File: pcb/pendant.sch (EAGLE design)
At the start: 55 parts, among them CON1 USB_MICROSMT+THRUHULE, Q2 16MHz, SW2 BUTTON_2, T1 SSM3J328R,LF, T2 SSM3J328R,LF, U2 MK20D--VFM5, U3 74LVC1G17DCK, U4 74LVC1G17DCK

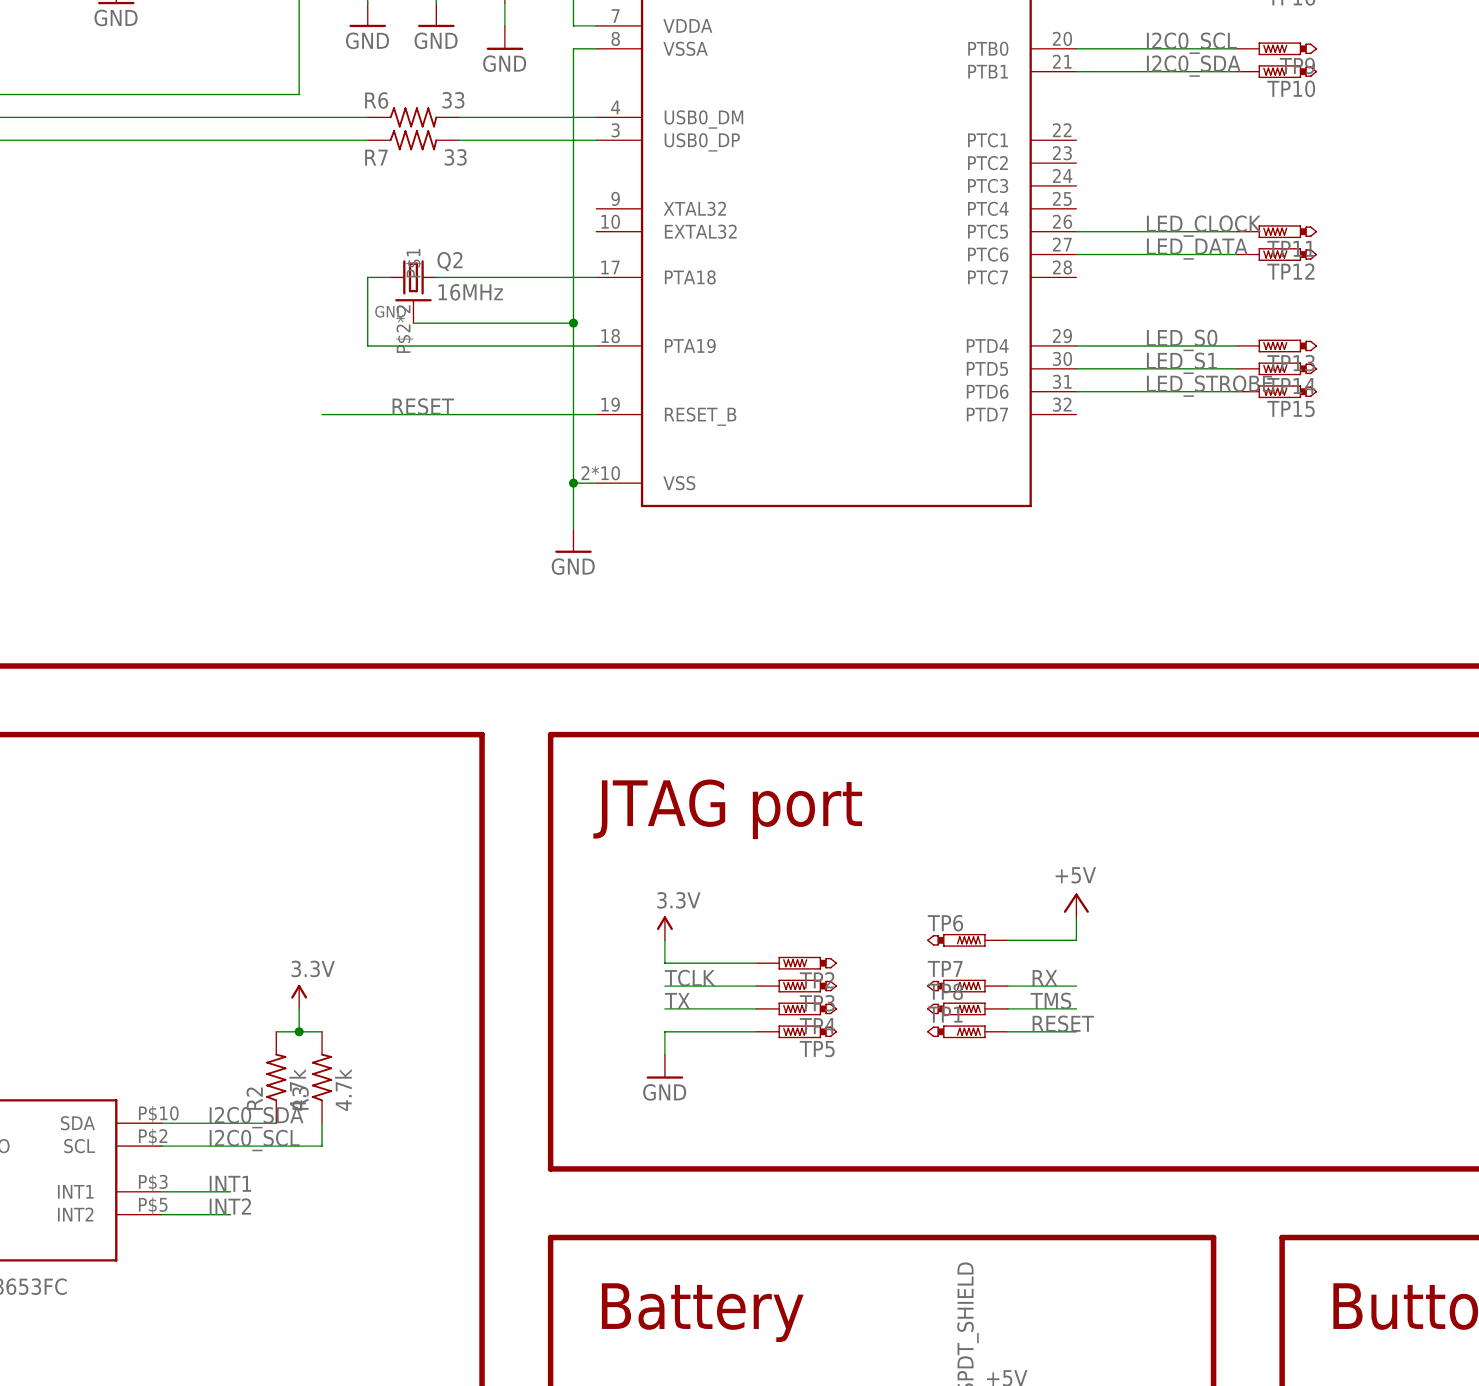
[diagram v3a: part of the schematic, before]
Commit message: Add interrupt line from accelerometer, clean up test pad positions
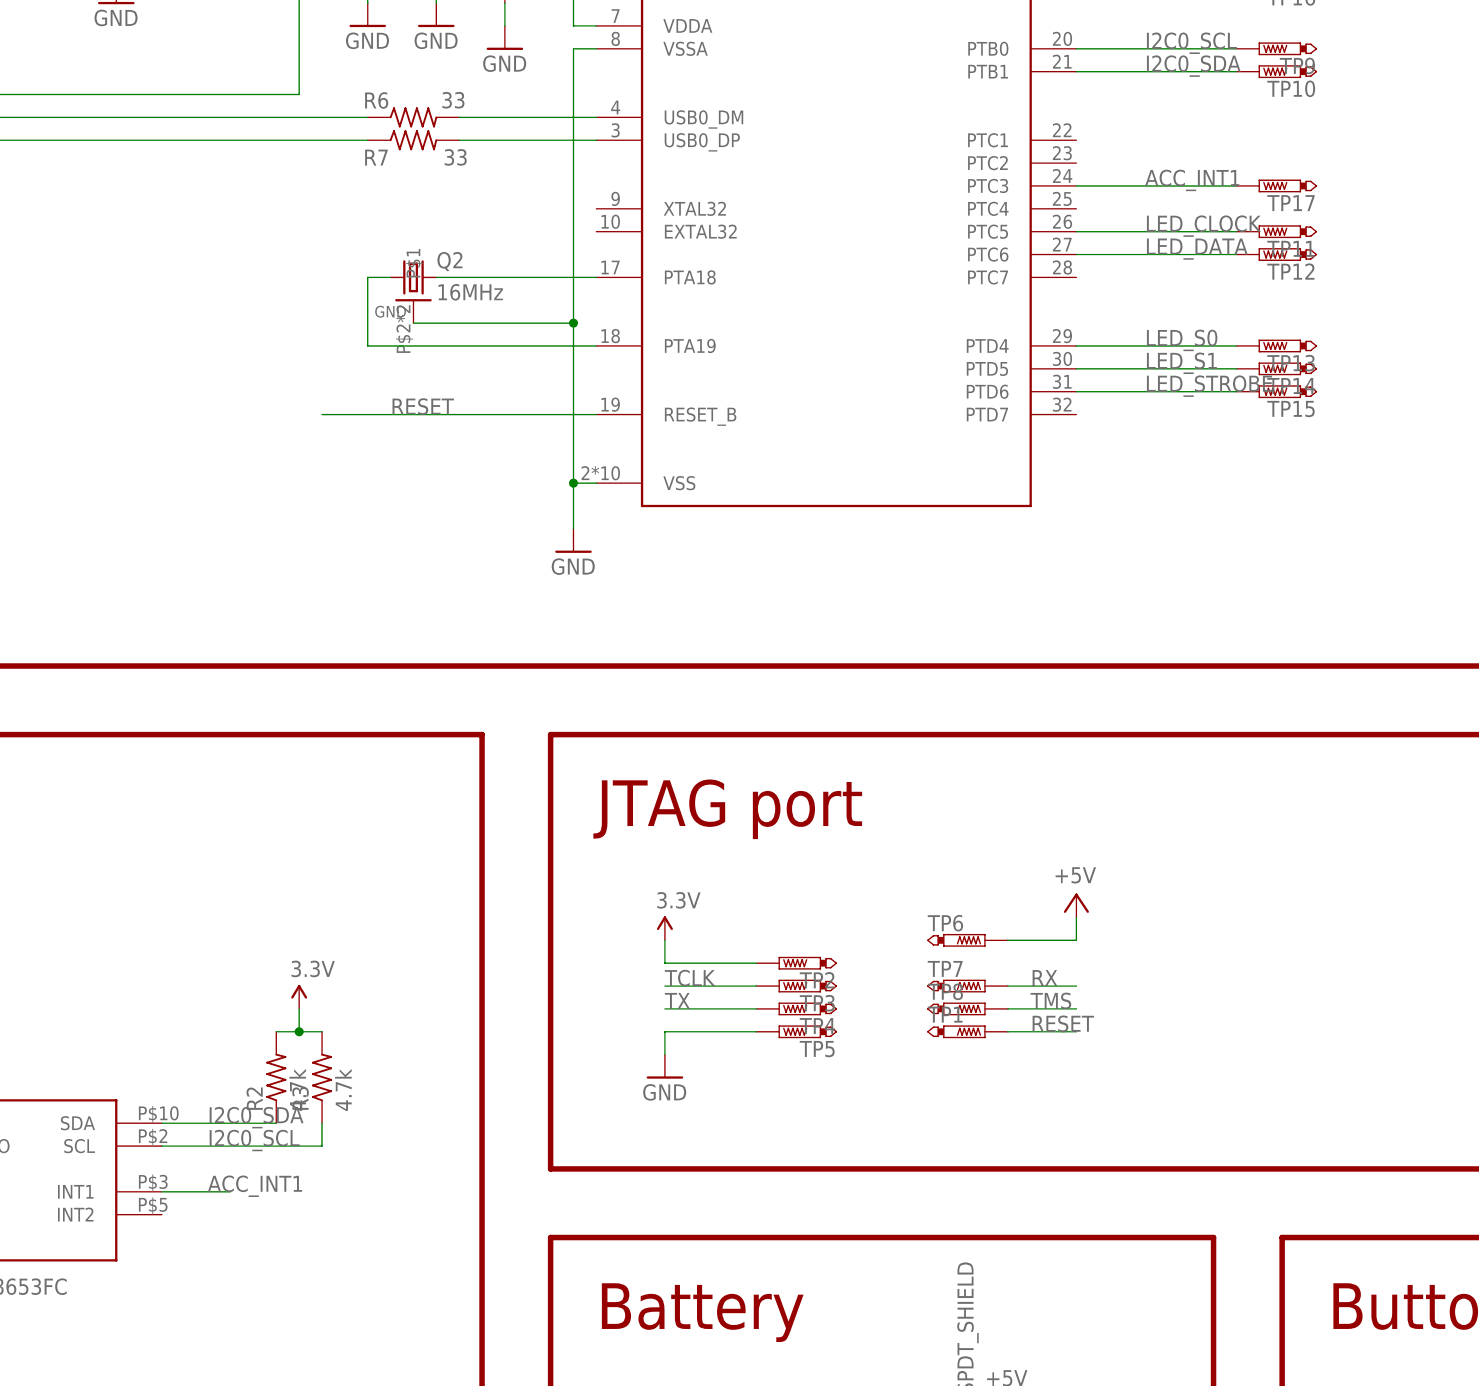
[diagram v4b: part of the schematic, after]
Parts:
- added TP17: PTR1B1,27, testpad:PTR1B1,27
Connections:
- removed net INT1: U$6.INT1
- removed net INT2: U$6.INT2
- new net ACC_INT1: TP17.TP, U$6.INT1, U2.PTC3
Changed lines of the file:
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@@
 <part name="TP16" library="testpad" deviceset="PTR1" device="B1,27"/>
 <part name="TP10" library="testpad" deviceset="PTR1" device="B1,27"/>
+<part name="TP17" library="testpad" deviceset="PTR1" device="B1,27"/>
 </parts>
 <sheets>
@@
 <instance part="TP16" gate="G$1" x="218.44" y="335.28" rot="R90"/>
 <instance part="TP10" gate="G$1" x="218.44" y="325.12" rot="R90"/>
+<instance part="TP17" gate="G$1" x="218.44" y="312.42" rot="R90"/>
 </instances>
 <busses>
@@
 </segment>
 </net>
-<net name="INT1" class="0">
+<net name="ACC_INT1" class="0">
+<segment>
+<pinref part="U2" gate="G$1" pin="PTC3"/>
+<wire x1="198.12" y1="312.42" x2="215.9" y2="312.42" width="0.1524" layer="91"/>
+<label x="205.74" y="312.42" size="1.778" layer="95"/>
+<pinref part="TP17" gate="G$1" pin="TP"/>
+</segment>
 <segment>
 <pinref part="U$6" gate="G$1" pin="INT1"/>
@@
 </segment>
 </net>
-<net name="INT2" class="0">
-<segment>
-<pinref part="U$6" gate="G$1" pin="INT2"/>
-<wire x1="96.52" y1="198.12" x2="104.14" y2="198.12" width="0.1524" layer="91"/>
-<label x="101.6" y="198.12" size="1.778" layer="95"/>
-</segment>
-</net>

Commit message: Update board
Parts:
- added TP18, TP19, TP20, TP21, TP22, TP23, TP24, TP25, TP26, TP27, TP28, TP29, TP30, TP31, TP32, TP33, TP34: PTR1B1,27, testpad:PTR1B1,27
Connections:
- removed net USB_SHIELD: CON1.SHIELD
- net B0: now also TP20.TP
- net B1: now also TP23.TP
- net B2: now also TP25.TP
- net B3: now also TP29.TP
- net B4: now also TP32.TP
- net G0: now also TP19.TP
- net G1: now also TP22.TP
- net G2: now also TP26.TP
- net G3: now also TP28.TP
- net G4: now also TP31.TP
- net GND: now also CON1.SHIELD
- net R0: now also TP18.TP
- net R1: now also TP21.TP
- net R2: now also TP24.TP
- net R3: now also TP27.TP
- net R4: now also TP30.TP
- net S0: now also TP33.TP
- net S1: now also TP34.TP
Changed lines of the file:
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@@
 <part name="TP10" library="testpad" deviceset="PTR1" device="B1,27"/>
 <part name="TP17" library="testpad" deviceset="PTR1" device="B1,27"/>
+<part name="TP18" library="testpad" deviceset="PTR1" device="B1,27"/>
+<part name="TP19" library="testpad" deviceset="PTR1" device="B1,27"/>
+<part name="TP20" library="testpad" deviceset="PTR1" device="B1,27"/>
+<part name="TP21" library="testpad" deviceset="PTR1" device="B1,27"/>
+<part name="TP22" library="testpad" deviceset="PTR1" device="B1,27"/>
+<part name="TP23" library="testpad" deviceset="PTR1" device="B1,27"/>
+<part name="TP24" library="testpad" deviceset="PTR1" device="B1,27"/>
+<part name="TP25" library="testpad" deviceset="PTR1" device="B1,27"/>
+<part name="TP26" library="testpad" deviceset="PTR1" device="B1,27"/>
+<part name="TP27" library="testpad" deviceset="PTR1" device="B1,27"/>
+<part name="TP28" library="testpad" deviceset="PTR1" device="B1,27"/>
+<part name="TP29" library="testpad" deviceset="PTR1" device="B1,27"/>
+<part name="TP30" library="testpad" deviceset="PTR1" device="B1,27"/>
+<part name="TP31" library="testpad" deviceset="PTR1" device="B1,27"/>
+<part name="TP32" library="testpad" deviceset="PTR1" device="B1,27"/>
+<part name="TP33" library="testpad" deviceset="PTR1" device="B1,27"/>
+<part name="TP34" library="testpad" deviceset="PTR1" device="B1,27"/>
 </parts>
 <sheets>
@@
 <instance part="TP10" gate="G$1" x="218.44" y="325.12" rot="R90"/>
 <instance part="TP17" gate="G$1" x="218.44" y="312.42" rot="R90"/>
+<instance part="TP18" gate="G$1" x="360.68" y="340.36" rot="R90"/>
+<instance part="TP19" gate="G$1" x="360.68" y="337.82" rot="R90"/>
+<instance part="TP20" gate="G$1" x="360.68" y="335.28" rot="R90"/>
+<instance part="TP21" gate="G$1" x="360.68" y="332.74" rot="R90"/>
+<instance part="TP22" gate="G$1" x="360.68" y="330.2" rot="R90"/>
+<instance part="TP23" gate="G$1" x="360.68" y="327.66" rot="R90"/>
+<instance part="TP24" gate="G$1" x="360.68" y="325.12" rot="R90"/>
+<instance part="TP25" gate="G$1" x="360.68" y="320.04" rot="R90"/>
+<instance part="TP26" gate="G$1" x="360.68" y="322.58" rot="R90"/>
+<instance part="TP27" gate="G$1" x="360.68" y="317.5" rot="R90"/>
+<instance part="TP28" gate="G$1" x="360.68" y="314.96" rot="R90"/>
+<instance part="TP29" gate="G$1" x="360.68" y="312.42" rot="R90"/>
+<instance part="TP30" gate="G$1" x="360.68" y="309.88" rot="R90"/>
+<instance part="TP31" gate="G$1" x="360.68" y="307.34" rot="R90"/>
+<instance part="TP32" gate="G$1" x="360.68" y="304.8" rot="R90"/>
+<instance part="TP33" gate="G$1" x="393.7" y="251.46" rot="R90"/>
+<instance part="TP34" gate="G$1" x="393.7" y="226.06" rot="R90"/>
 </instances>
 <busses>
@@
 <label x="386.08" y="251.46" size="1.778" layer="95"/>
 <pinref part="T1" gate="A" pin="D"/>
+<pinref part="TP33" gate="G$1" pin="TP"/>
 </segment>
 <segment>
@@
 <label x="386.08" y="226.06" size="1.778" layer="95"/>
 <pinref part="T2" gate="A" pin="D"/>
+<pinref part="TP34" gate="G$1" pin="TP"/>
 </segment>
 <segment>
@@
 <wire x1="350.52" y1="340.36" x2="358.14" y2="340.36" width="0.1524" layer="91"/>
 <label x="353.06" y="340.36" size="1.778" layer="95"/>
+<pinref part="TP18" gate="G$1" pin="TP"/>
 </segment>
 </net>
@@
 <wire x1="350.52" y1="332.74" x2="358.14" y2="332.74" width="0.1524" layer="91"/>
 <label x="353.06" y="332.74" size="1.778" layer="95"/>
+<pinref part="TP21" gate="G$1" pin="TP"/>
 </segment>
 </net>
@@
 <wire x1="358.14" y1="325.12" x2="350.52" y2="325.12" width="0.1524" layer="91"/>
 <label x="353.06" y="325.12" size="1.778" layer="95"/>
+<pinref part="TP24" gate="G$1" pin="TP"/>
 </segment>
 </net>
@@
 <wire x1="350.52" y1="317.5" x2="358.14" y2="317.5" width="0.1524" layer="91"/>
 <label x="353.06" y="317.5" size="1.778" layer="95"/>
+<pinref part="TP27" gate="G$1" pin="TP"/>
 </segment>
 </net>
@@
 <wire x1="358.14" y1="304.8" x2="350.52" y2="304.8" width="0.1524" layer="91"/>
 <label x="353.06" y="304.8" size="1.778" layer="95"/>
+<pinref part="TP32" gate="G$1" pin="TP"/>
 </segment>
 <segment>
@@
 <wire x1="350.52" y1="307.34" x2="358.14" y2="307.34" width="0.1524" layer="91"/>
 <label x="353.06" y="307.34" size="1.778" layer="95"/>
+<pinref part="TP31" gate="G$1" pin="TP"/>
 </segment>
 <segment>
@@
 <wire x1="350.52" y1="312.42" x2="358.14" y2="312.42" width="0.1524" layer="91"/>
 <label x="353.06" y="312.42" size="1.778" layer="95"/>
+<pinref part="TP29" gate="G$1" pin="TP"/>
 </segment>
 </net>
@@
 <wire x1="358.14" y1="314.96" x2="350.52" y2="314.96" width="0.1524" layer="91"/>
 <label x="353.06" y="314.96" size="1.778" layer="95"/>
+<pinref part="TP28" gate="G$1" pin="TP"/>
 </segment>
 </net>
@@
 <wire x1="358.14" y1="330.2" x2="350.52" y2="330.2" width="0.1524" layer="91"/>
 <label x="353.06" y="330.2" size="1.778" layer="95"/>
+<pinref part="TP22" gate="G$1" pin="TP"/>
 </segment>
 </net>
@@
 <wire x1="350.52" y1="327.66" x2="358.14" y2="327.66" width="0.1524" layer="91"/>
 <label x="353.06" y="327.66" size="1.778" layer="95"/>
+<pinref part="TP23" gate="G$1" pin="TP"/>
 </segment>
 </net>
@@
 <wire x1="350.52" y1="322.58" x2="358.14" y2="322.58" width="0.1524" layer="91"/>
 <label x="353.06" y="322.58" size="1.778" layer="95"/>
+<pinref part="TP26" gate="G$1" pin="TP"/>
 </segment>
 </net>
@@
 <wire x1="358.14" y1="320.04" x2="350.52" y2="320.04" width="0.1524" layer="91"/>
 <label x="353.06" y="320.04" size="1.778" layer="95"/>
+<pinref part="TP25" gate="G$1" pin="TP"/>
 </segment>
 </net>
@@
 <wire x1="350.52" y1="337.82" x2="358.14" y2="337.82" width="0.1524" layer="91"/>
 <label x="353.06" y="337.82" size="1.778" layer="95"/>
+<pinref part="TP19" gate="G$1" pin="TP"/>
 </segment>
 </net>
@@
 <wire x1="358.14" y1="335.28" x2="350.52" y2="335.28" width="0.1524" layer="91"/>
 <label x="353.06" y="335.28" size="1.778" layer="95"/>
+<pinref part="TP20" gate="G$1" pin="TP"/>
 </segment>
 </net>
@@
 <segment>
 <pinref part="GND1" gate="1" pin="GND"/>
-<wire x1="60.96" y1="312.42" x2="60.96" y2="284.48" width="0.1524" layer="91"/>
+<wire x1="60.96" y1="312.42" x2="60.96" y2="307.34" width="0.1524" layer="91"/>
 <pinref part="CON1" gate="G$1" pin="GND"/>
+<wire x1="60.96" y1="307.34" x2="60.96" y2="284.48" width="0.1524" layer="91"/>
 <wire x1="53.34" y1="312.42" x2="60.96" y2="312.42" width="0.1524" layer="91"/>
+<pinref part="CON1" gate="G$1" pin="SHIELD"/>
+<wire x1="53.34" y1="307.34" x2="60.96" y2="307.34" width="0.1524" layer="91"/>
+<junction x="60.96" y="307.34"/>
 </segment>
 <segment>
@@
 </segment>
 </net>
-<net name="USB_SHIELD" class="0">
-<segment>
-<pinref part="CON1" gate="G$1" pin="SHIELD"/>
-<wire x1="53.34" y1="307.34" x2="53.34" y2="297.18" width="0.1524" layer="91"/>
-<wire x1="53.34" y1="297.18" x2="38.1" y2="297.18" width="0.1524" layer="91"/>
-<label x="38.1" y="297.18" size="1.778" layer="95"/>
-</segment>
-</net>
 <net name="R4" class="0">
 <segment>
@@
 <wire x1="358.14" y1="309.88" x2="350.52" y2="309.88" width="0.1524" layer="91"/>
 <label x="353.06" y="309.88" size="1.778" layer="95"/>
-</segment>
-<segment>
+<pinref part="TP30" gate="G$1" pin="TP"/>
+</segment>
+<segment>
